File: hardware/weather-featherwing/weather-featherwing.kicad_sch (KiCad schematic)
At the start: 33 parts, among them J1 Feather_Header_01x16, J2 Feather_Header_01x12, J3 MEM2061, J4 STEMMA-QT, SW1 JS102011SAQN, U1 LPS22HB, U2 SHT41, U3 11AA010

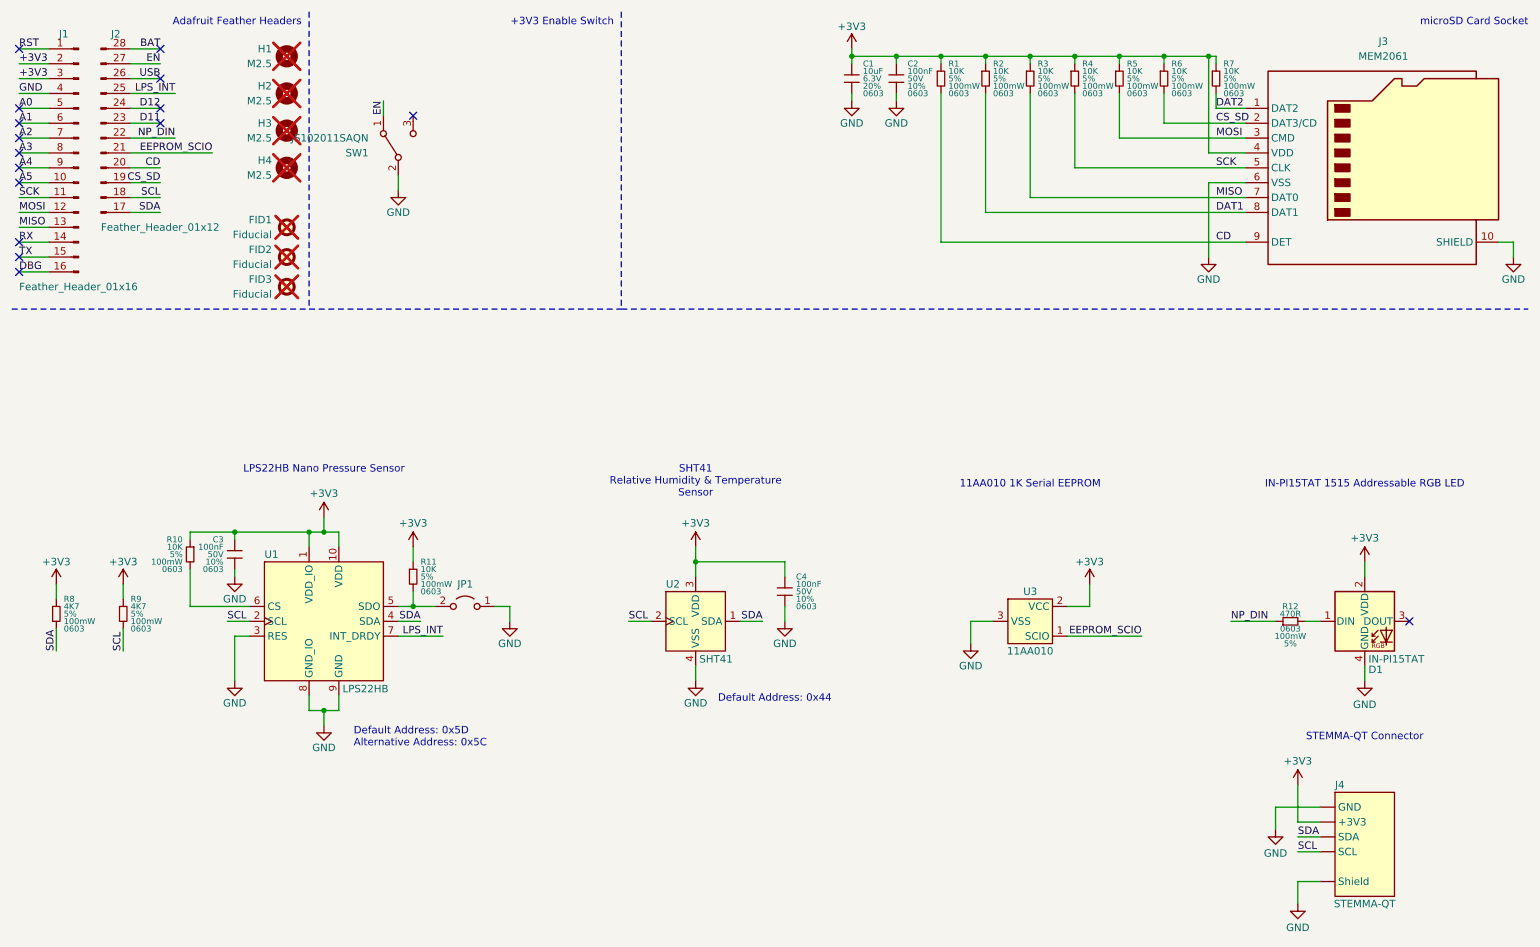
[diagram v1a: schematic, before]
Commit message: blender renders and cleaned up files
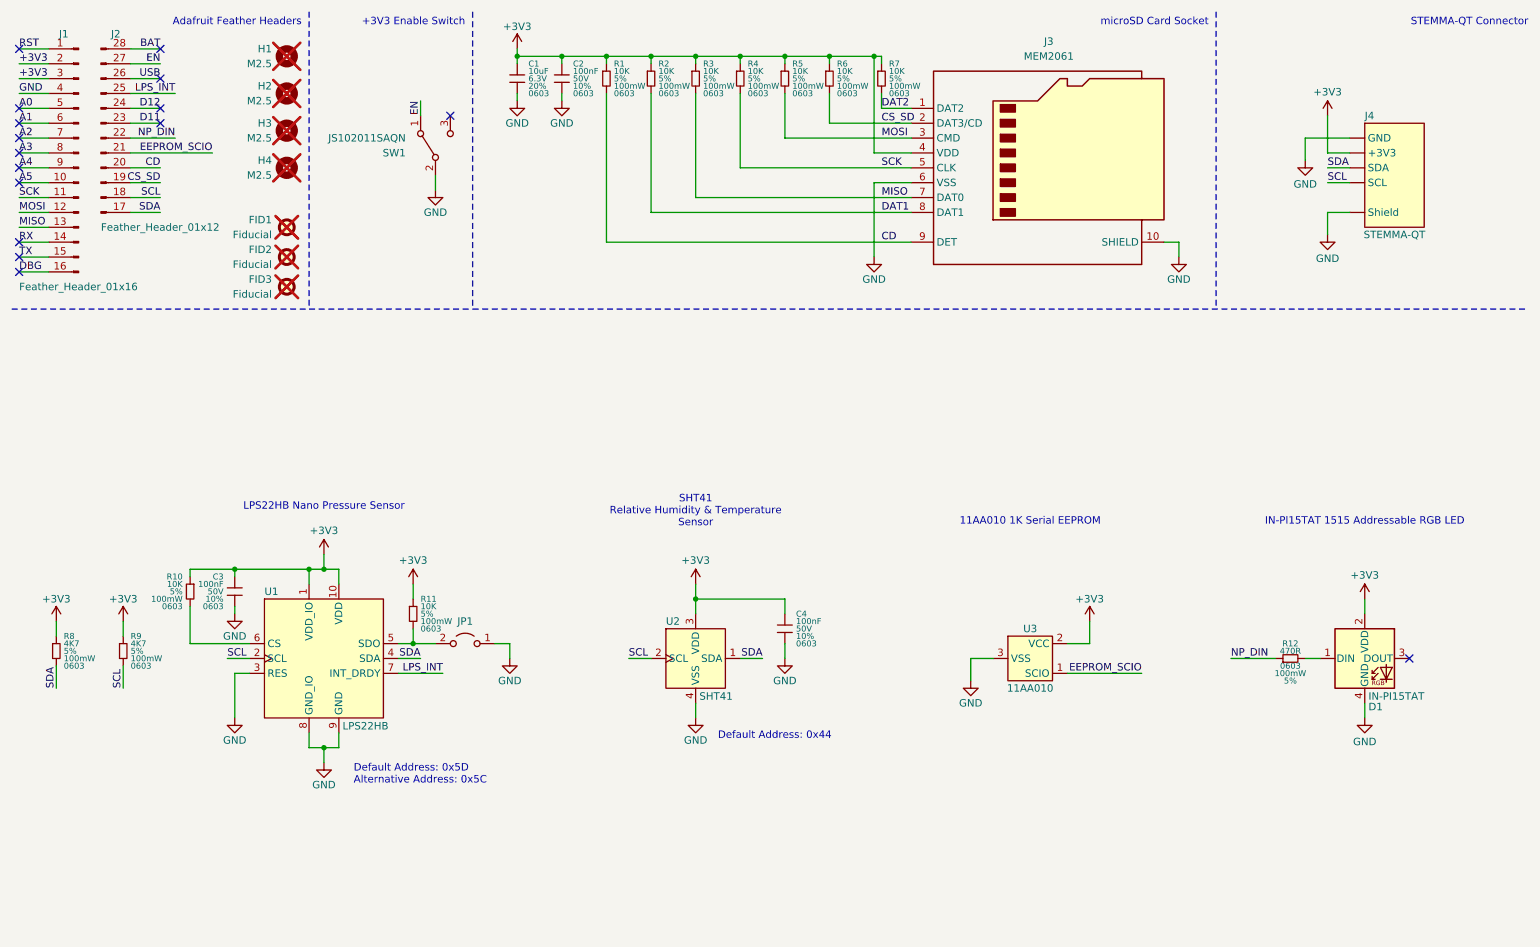
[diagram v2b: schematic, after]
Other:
- note added: "STEMMA-QT Connector"
- title: Weather Featherwing v1.2.1 -> Weather Featherwing v1.2.2
- moved on the sheet: C1, C2, C3, C4, D1, J3, J4, JP1, R1, R10, R11, R12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

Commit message: housekeeping
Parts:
- U1: mpn LPS2x -> LPS22HBTR
- U2: footprint DS-Master-Sensors-SMD:SHT4x -> lib_fp:SHT4x
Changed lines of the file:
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@@
       (effects (font (size 1.27 1.27)) hide)
     )
-    (property "mpn" "LPS2x" (at 63.5 120.65 0)
+    (property "mpn" "LPS22HBTR" (at 63.5 120.65 0)
       (effects (font (size 1.27 1.27)) hide)
     )
@@
       (effects (font (size 1.27 1.27)) (justify left top))
     )
-    (property "Footprint" "DS-Master-Sensors-SMD:SHT4x" (at 127 120.65 0)
-      (effects (font (size 1.27 1.27)) hide)
-    )
+    (property "Footprint" "lib_fp:SHT4x" (at 127 120.65 0)
+      (effects (font (size 1.27 1.27)) hide)
+    )

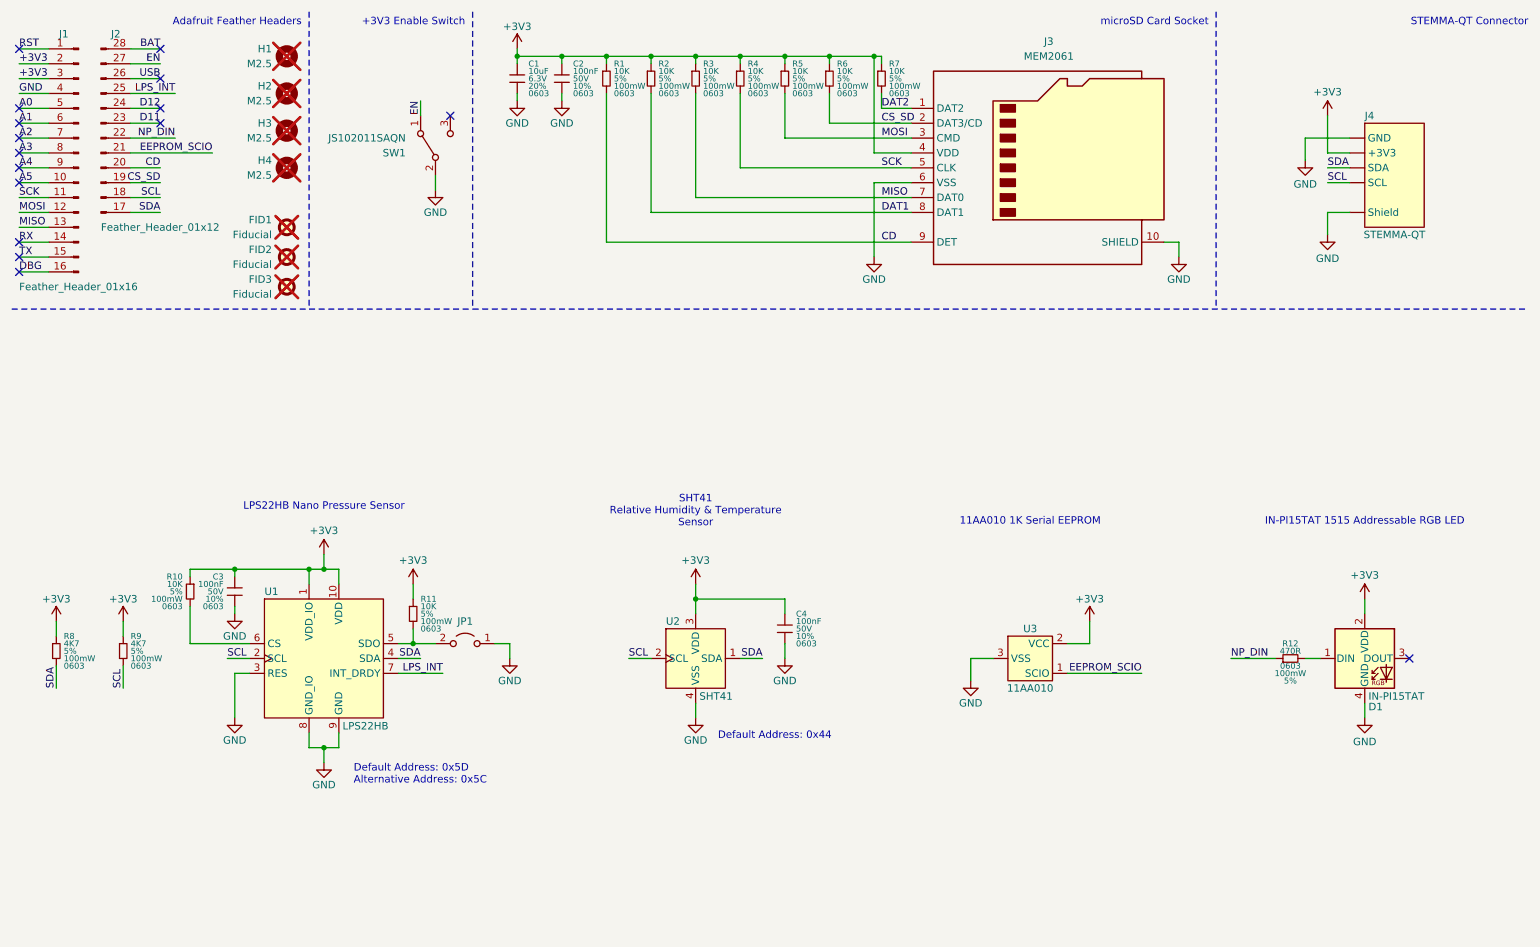
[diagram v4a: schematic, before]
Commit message: updated schematic refs
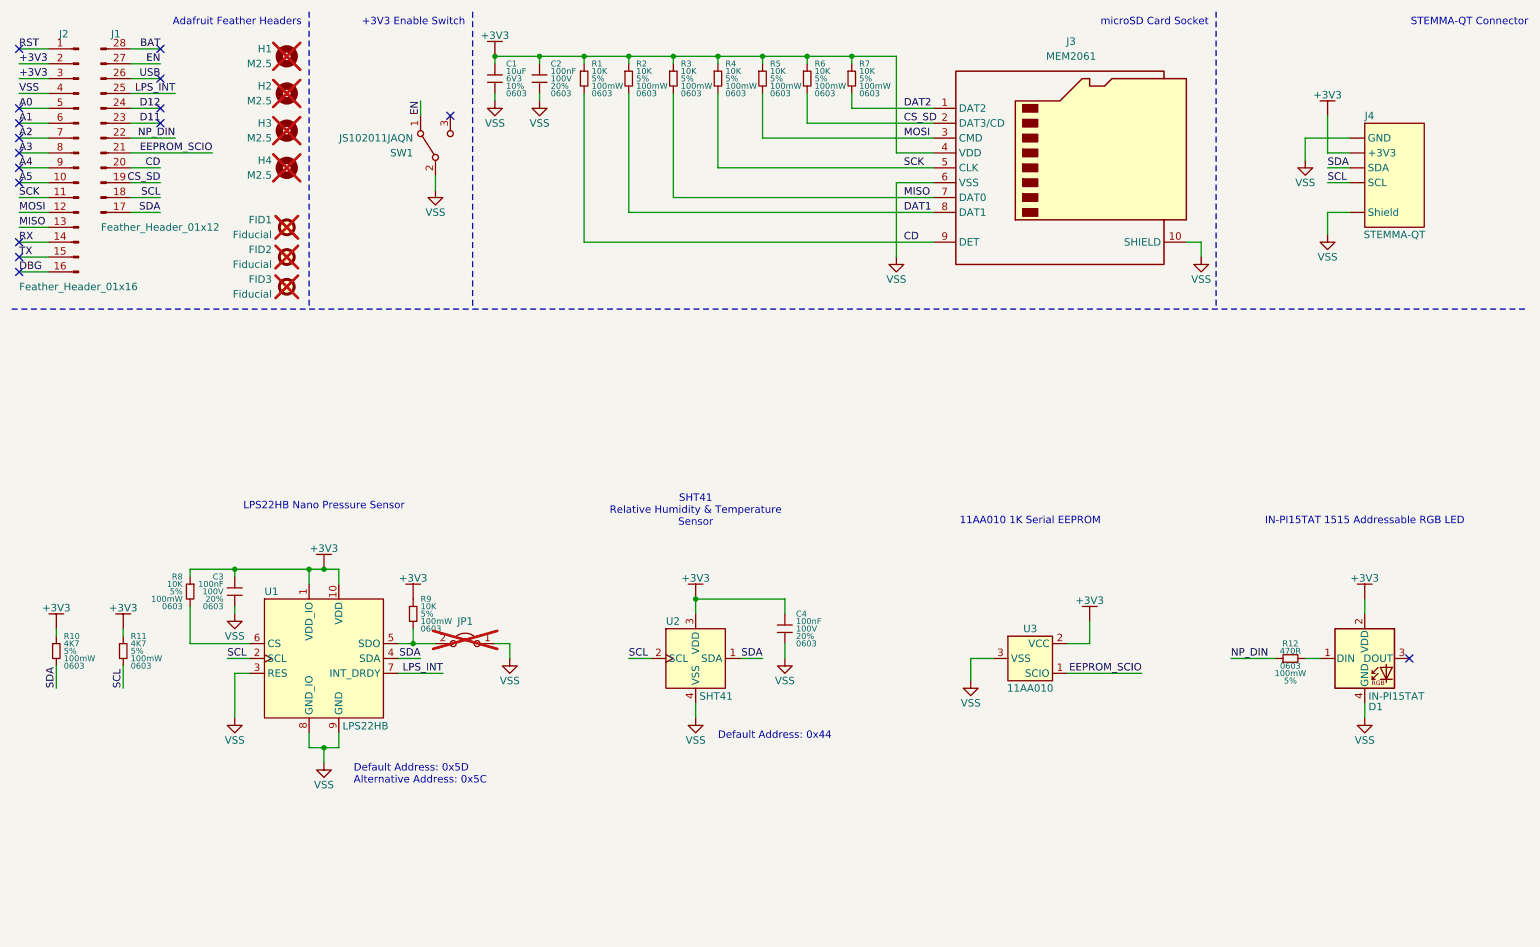
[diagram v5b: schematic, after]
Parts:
- removed R1, R11, R2, R3, R4, R5, R6, R7: 10K, lib_fp:RESC160X80X55L30N, symbol lib_sch:r_small
- removed R8: 4K7, lib_fp:RESC160X80X55L30N, symbol lib_sch:r_small
- added R1, R2, R3, R4, R5, R6, R7, R8, R9: 10K, lib_fp:CRCW0603, symbol lib_sch:R
- C1: footprint lib_fp:CAPC160X80X88L35N -> lib_fp:GRT0603; DKPN (none) -> 490-12538-1-ND; MPN (none) -> GRM188R60J106KE47D; Manufacturer KYOCERA AVX -> Murata Electronics; Tolerance 20% -> 10%; Voltage Rating 6.3V -> 6V3; mpn KGM15CR50J106MT -> (none); populate 1 -> (none)
- C2, C3, C4: footprint lib_fp:CAPC160X80X88L35N -> lib_fp:GRT0603; DKPN (none) -> 490-16327-1-ND; MPN (none) -> GRM188R72A104MA35D; Manufacturer KYOCERA AVX -> Murata Electronics; Tolerance 10% -> 20%; Voltage Rating 50V -> 100V; mpn KGM15AR51H104KT -> (none); populate 1 -> (none)
- D1: DKPN (none) -> 1830-IN-PI15TAT5R5G5BCT-ND; MPN (none) -> IN-PI15TAT5R5G5B; mpn IN-PI15TAT5R5G5B -> (none); populate 1 -> (none)
- H1, H2, H3, H4: populate 0 -> (none)
- J1: renamed from J2; DKPN (none) -> S1012EC-12-ND; MPN (none) -> PREC012SAAN-RC; mpn PREC012SAAN-RC -> (none); populate 0 -> (none)
- J2: renamed from J1; DKPN (none) -> S1012EC-16-ND; MPN (none) -> PREC016SAAN-RC; mpn PREC016SAAN-RC -> (none); populate 0 -> (none)
- J3: DKPN (none) -> 2073-MEM2061-01-188-00-ACT-ND; MPN (none) -> MEM2061-01-188-00-A; mpn MEM2061-01-188-00-A -> (none); populate 1 -> (none)
- J4: DKPN (none) -> 455-SM04B-SRSS-TBCT-ND; MPN (none) -> SM04B-SRSS-TB; mpn SM04B-SRSS-TB -> (none); populate 1 -> (none)
- JP1: populate 0 -> (none); now not fitted
- R10: value 10K -> 4K7; footprint lib_fp:RESC160X80X55L30N -> lib_fp:CRCW0603; DKPN (none) -> 541-4.7KGCT-ND; mpn CRCW060310K0JNEB -> CRCW06034K70JNEA; populate 1 -> (none)
- R11: renamed from R9; footprint lib_fp:RESC160X80X55L30N -> lib_fp:CRCW0603; DKPN (none) -> 541-4.7KGCT-ND; populate 1 -> (none)
- R12: footprint lib_fp:RESC160X80X55L30N -> lib_fp:CRCW0603; DKPN (none) -> 541-CRCW0603470RJNEBCT-ND; populate 1 -> (none)
- SW1: value JS102011SAQN -> JS102011JAQN; footprint lib_fp:JS102011SAQN -> lib_fp:JS102011JAQN; DKPN (none) -> CKN10720CT-ND; MPN (none) -> JS102011JAQN; mpn JS102011SAQN -> (none); populate 1 -> (none)
- U1: DKPN (none) -> 497-16265-1-ND; populate 1 -> (none)
- U2: DKPN (none) -> 1649-SHT41-AD1F-R2CT-ND; MPN (none) -> SHT41-AD1F-R2; mpn SHT41-AD1B-R3 -> (none); populate 1 -> (none)
- U3: DKPN (none) -> 11AA010T-I/TTCT-ND; MPN (none) -> 11AA010T-I/TT; mpn 11AA010T-I/TT -> (none); populate 1 -> (none)
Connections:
- net +3V3: now also R1.1, R2.1, R3.1, R4.1, R5.1, R6.1, R7.1, R8.1, R9.1
- net CD: now also R1.2
- net CS_SD: now also R6.2
- net DAT1: now also R2.2
- net DAT2: now also R7.2
- net MISO: now also R3.2
- net MOSI: now also R5.2
- net SCK: now also R4.2
- net SDA: now also R10.2
- net at JP1.2 (B), U1.5 (SDO): now also R9.2
- net at U1.6 (CS): now also R8.2; no longer R10.2
- net GND renamed VSS
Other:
- moved on the sheet: C1, C2, J3
